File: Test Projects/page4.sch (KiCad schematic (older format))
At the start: 12 parts, among them U7 2N168

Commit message: Continued proto 1 layout
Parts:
- added C36: C, Capacitors_Tantalum_SMD:TantalC_SizeB_EIA-3528_Reflow, symbol C
- added P27, P28, P29, P30, P31, P32: CONN_01X06, Pin_Headers:Pin_Header_Straight_1x06, symbol CONN_01X06
- added R11, R12, R13, R14, R15: R, Resistors_SMD:R_0603, symbol R
- added U28, U29: SF-74x125, SparkFun-Footprints:SF-SOT-23-5, symbol SF-74x125
- added U30: SF-LM358, SparkFun-Footprints:SF-SOIC-8, symbol SF-LM358
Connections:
- net at JACK3.4: now also R11.2
- net at JACK3.5: now also R13.1
- net at JACK4.4: now also R12.2
- net at JACK4.5: now also R14.1
- net GND: now reaches U7.5 (GND)
- net GND: now also C36.1, U28.1 (/OE), U28.3 (GND), U29.1 (/OE), U29.3 (GND), U30.4 (V-)
- net PORT-TX: now reaches U7.6 (Vo)
- net PORT-TX: now also R15.2, U28.2 (A)
- net +5V: now reaches U7.8 (VCC)
- net +5V: now also C36.2, R11.1, R12.1, R15.1, U28.5 (VCC), U29.5 (VCC), U30.8 (V+)
- net at JACK5.G: now also P27.5 (P5)
- net at JACK5.R: now also P27.2 (P2)
- net at JACK5.RN: now also P27.1 (P1)
- net at JACK5.S: now also P27.6 (P6)
- net at JACK5.T: now also P27.4 (P4)
- net at JACK5.TN: now also P27.3 (P3)
- net at JACK6.G: now also P28.5 (P5)
- net at JACK6.R: now also P28.2 (P2)
- net at JACK6.RN: now also P28.1 (P1)
- net at JACK6.S: now also P28.6 (P6)
- net at JACK6.T: now also P28.4 (P4)
- net at JACK6.TN: now also P28.3 (P3)
- net at JACK7.G: now also P29.5 (P5)
- net at JACK7.R: now also P29.2 (P2)
- net at JACK7.RN: now also P29.1 (P1)
- net at JACK7.S: now also P29.6 (P6)
- net at JACK7.T: now also P29.4 (P4)
- net at JACK7.TN: now also P29.3 (P3)
- net at JACK8.G: now also P30.5 (P5)
- net at JACK8.R: now also P30.2 (P2)
- net at JACK8.RN: now also P30.1 (P1)
- net at JACK8.S: now also P30.6 (P6)
- net at JACK8.T: now also P30.4 (P4)
- net at JACK8.TN: now also P30.3 (P3)
- net at JACK9.G: now also P31.5 (P5)
- net at JACK9.R: now also P31.2 (P2)
- net at JACK9.RN: now also P31.1 (P1)
- net at JACK9.S: now also P31.6 (P6)
- net at JACK9.T: now also P31.4 (P4)
- net at JACK9.TN: now also P31.3 (P3)
- net at JACK10.G: now also P32.5 (P5)
- net at JACK10.R: now also P32.2 (P2)
- net at JACK10.RN: now also P32.1 (P1)
- net at JACK10.S: now also P32.6 (P6)
- net at JACK10.T: now also P32.4 (P4)
- net at JACK10.TN: now also P32.3 (P3)
- new net: R13.2, U28.4 (Y)
- new net: R14.2, U29.4 (Y)
- new net PORT-RX: U29.2 (A)
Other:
- moved on the sheet: JACK3, JACK4, U7

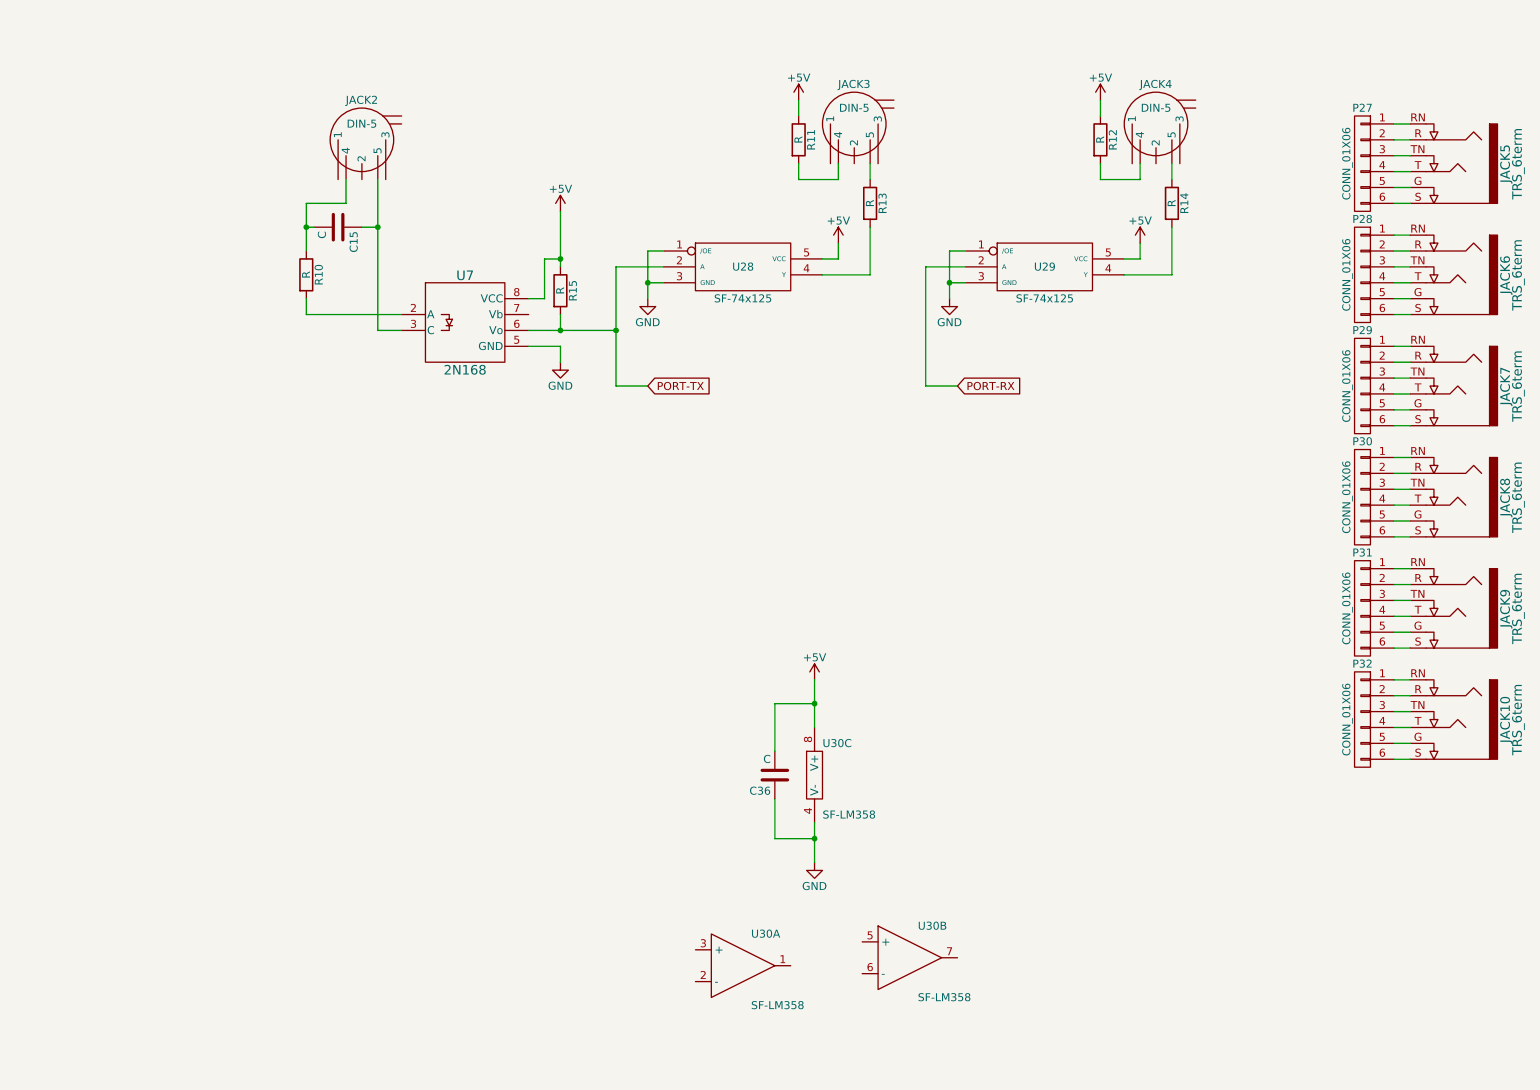
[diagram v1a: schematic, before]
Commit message: Moved to 10x5 size
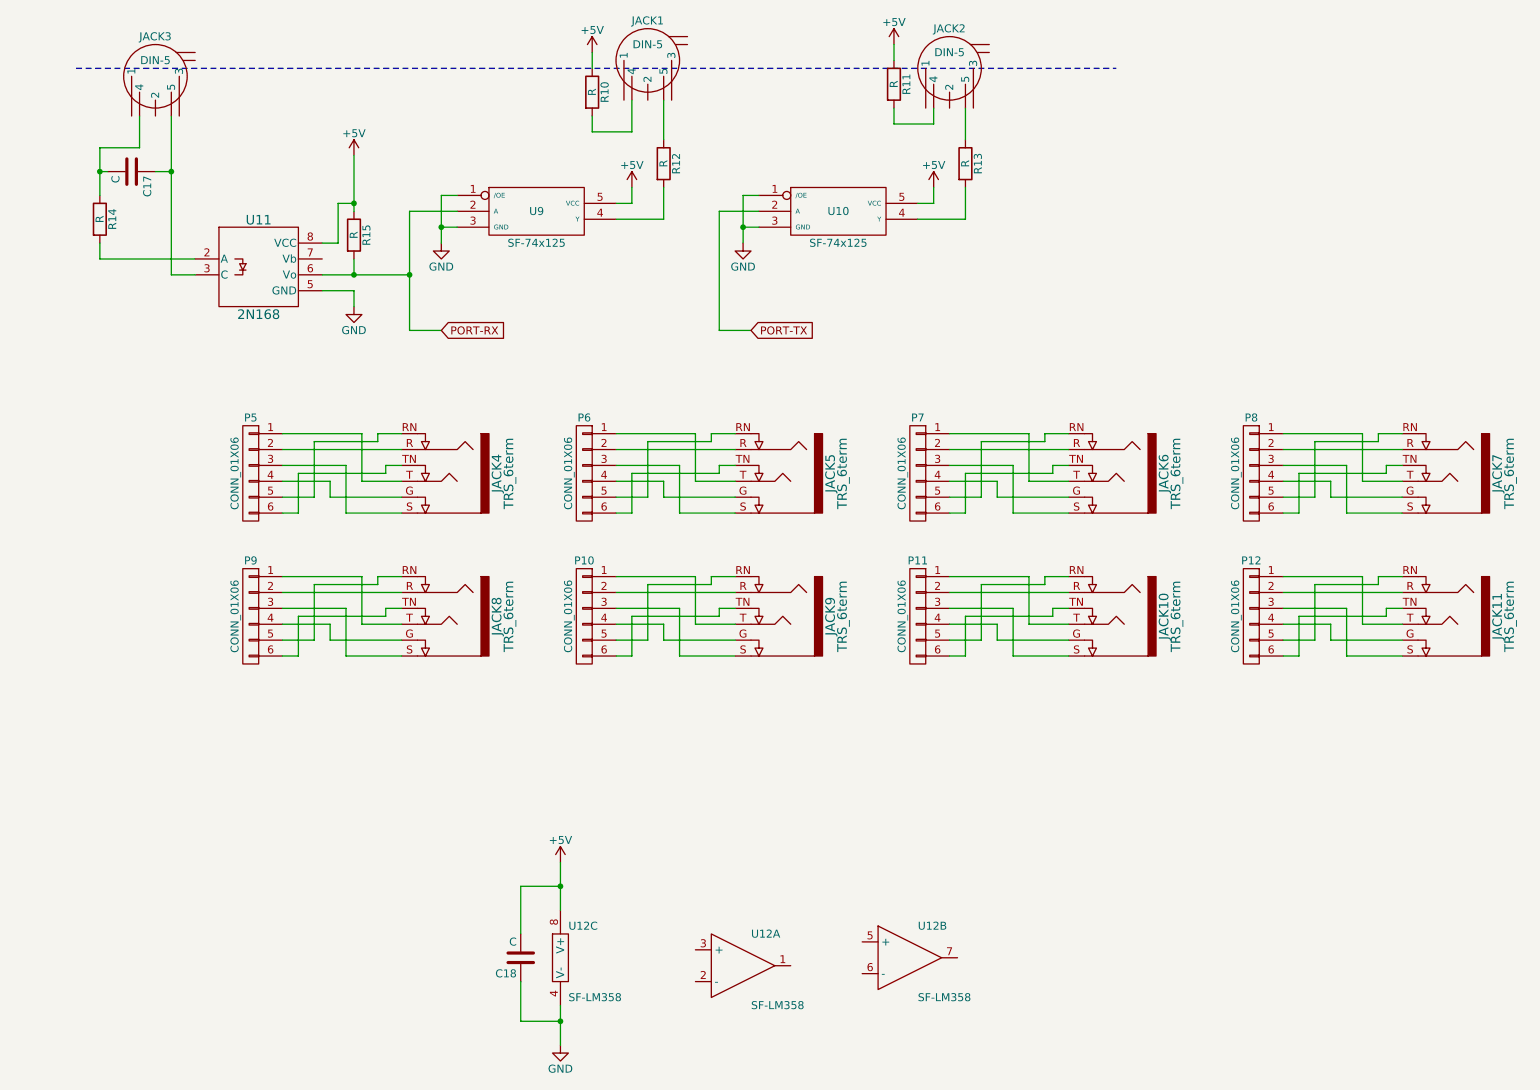
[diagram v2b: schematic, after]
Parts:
- removed P28, P29, P30, P31, P32: CONN_01X06, Pin_Headers:Pin_Header_Straight_1x06, symbol CONN_01X06
- added JACK11, JACK5: TRS_6term, SparkFun-Footprints:SF-Neutrik-Jack-6-term, symbol TRS_6term
- added P10, P11, P12, P6, P7, P8, P9: CONN_01X06, Pin_Headers:Pin_Header_Straight_1x06, symbol CONN_01X06
- renumbered C15 to C17, C36 to C18, JACK3 to JACK1, JACK4 to JACK2, JACK2 to JACK3, JACK5 to JACK4, P27 to P5, R11 to R10, R12 to R11, R13 to R12, R14 to R13, R10 to R14, U29 to U10, U7 to U11, U30 to U12, U28 to U9
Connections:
- net PORT-RX: now also R15.2, U11.6 (Vo), U9.2 (A); no longer U10.2 (A)
- net PORT-TX: now also U10.2 (A); no longer R15.2, U11.6 (Vo), U9.2 (A)
- net at JACK4.G: now also P5.4 (P4); no longer P5.5 (P5)
- net at JACK4.RN: now also P5.5 (P5); no longer P5.1 (P1)
- net at JACK4.S: now also P5.3 (P3); no longer P5.6 (P6)
- net at JACK4.T: now also P5.1 (P1); no longer P5.4 (P4)
- net at JACK4.TN: now also P5.6 (P6); no longer P5.3 (P3)
- net at JACK6.G: now also P7.4 (P4)
- net at JACK6.R: now also P7.2 (P2)
- net at JACK6.RN: now also P7.5 (P5)
- net at JACK6.S: now also P7.3 (P3)
- net at JACK6.T: now also P7.1 (P1)
- net at JACK6.TN: now also P7.6 (P6)
- net at JACK7.G: now also P8.4 (P4)
- net at JACK7.R: now also P8.2 (P2)
- net at JACK7.RN: now also P8.5 (P5)
- net at JACK7.S: now also P8.3 (P3)
- net at JACK7.T: now also P8.1 (P1)
- net at JACK7.TN: now also P8.6 (P6)
- net at JACK8.G: now also P9.4 (P4)
- net at JACK8.R: now also P9.2 (P2)
- net at JACK8.RN: now also P9.5 (P5)
- net at JACK8.S: now also P9.3 (P3)
- net at JACK8.T: now also P9.1 (P1)
- net at JACK8.TN: now also P9.6 (P6)
- net at JACK9.G: now also P10.4 (P4)
- net at JACK9.R: now also P10.2 (P2)
- net at JACK9.RN: now also P10.5 (P5)
- net at JACK9.S: now also P10.3 (P3)
- net at JACK9.T: now also P10.1 (P1)
- net at JACK9.TN: now also P10.6 (P6)
- net at JACK10.G: now also P11.4 (P4)
- net at JACK10.R: now also P11.2 (P2)
- net at JACK10.RN: now also P11.5 (P5)
- net at JACK10.S: now also P11.3 (P3)
- net at JACK10.T: now also P11.1 (P1)
- net at JACK10.TN: now also P11.6 (P6)
- new net: JACK5.G, P6.4 (P4)
- new net: JACK5.R, P6.2 (P2)
- new net: JACK5.RN, P6.5 (P5)
- new net: JACK5.S, P6.3 (P3)
- new net: JACK5.T, P6.1 (P1)
- new net: JACK5.TN, P6.6 (P6)
- new net: JACK11.G, P12.4 (P4)
- new net: JACK11.R, P12.2 (P2)
- new net: JACK11.RN, P12.5 (P5)
- new net: JACK11.S, P12.3 (P3)
- new net: JACK11.T, P12.1 (P1)
- new net: JACK11.TN, P12.6 (P6)
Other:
- moved on the sheet: C17, C18, JACK1, JACK2, JACK3, JACK4, P5, R10, R11, R12, R13, R14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

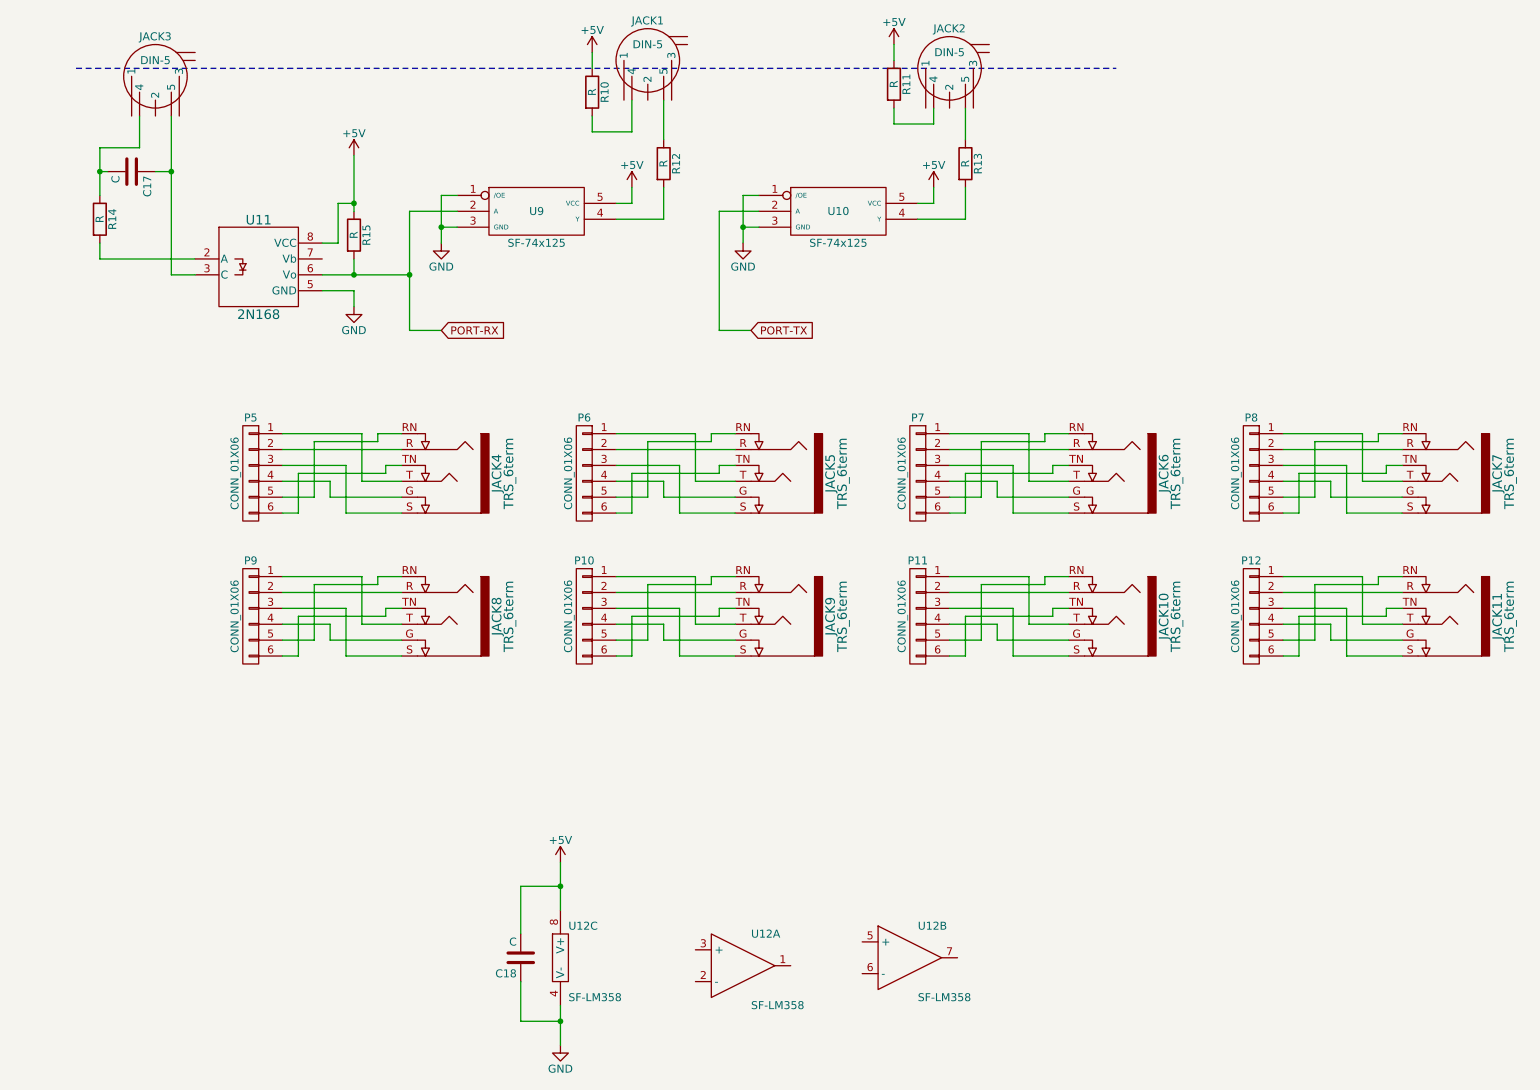
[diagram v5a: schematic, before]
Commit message: Added holes, moved layout
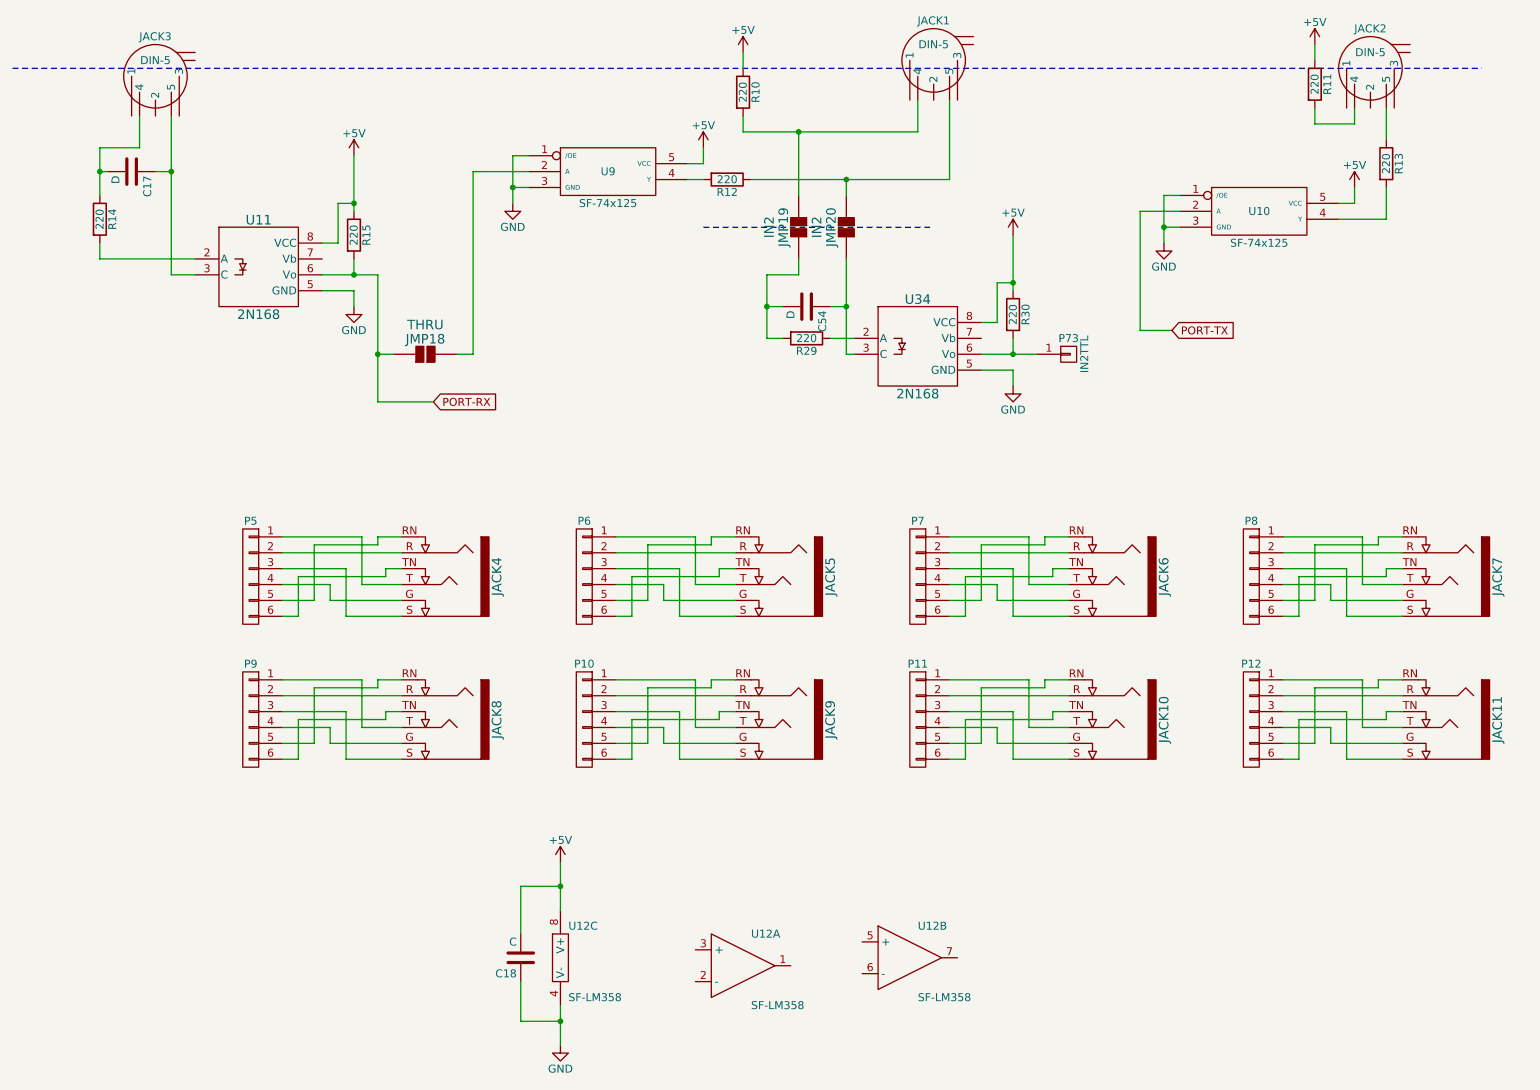
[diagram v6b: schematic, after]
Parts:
- added C54: D, Capacitors_Tantalum_SMD:TantalC_SizeB_EIA-3528_Reflow, symbol C
- added JMP18: THRU, SparkFun-Footprints:SF-2way-open, symbol 2Jumper
- added JMP19, JMP20: IN2, SparkFun-Footprints:SF-2way-open, symbol 2Jumper
- added P73: IN2TTL, SparkFun-Footprints:TestHole, symbol CONN_01X01
- added R29, R30: 220, Resistors_SMD:R_0603, symbol R
- added U34: 2N168, SparkFun-Footprints:SF-SMD-8, symbol 2N168
- C17: value C -> D
- R10, R11, R12, R13, R14, R15: value R -> 220
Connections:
- net +5V: now also R30.1, U34.8 (VCC)
- net GND: now also U34.5 (GND)
- net PORT-RX: now also JMP18.1; no longer U9.2 (A)
- net at JACK1.4, R10.2: now also JMP19.2
- net at JACK1.5, R12.1: now also JMP20.2
- new net: JMP18.2, U9.2 (A)
- new net: C54.1, JMP20.1, U34.3 (C)
- new net: C54.2, JMP19.1, R29.2
- new net: R29.1, U34.2 (A)
- new net: P73.1 (P1), R30.2, U34.6 (Vo)
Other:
- moved on the sheet: JACK1, JACK10, JACK11, JACK2, JACK4, JACK5, JACK6, JACK7, JACK8, JACK9, P10, P11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

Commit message: Routing, 15%
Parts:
- removed C18: C, Capacitors_Tantalum_SMD:TantalC_SizeB_EIA-3528_Reflow, symbol C
- removed U12: SF-LM358, SparkFun-Footprints:SF-SOIC-8, symbol SF-LM358
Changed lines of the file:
@@
 EESchema Schematic File Version 2
+LIBS:Teensy_test_layout-rescue
 LIBS:power
 LIBS:device
@@
 LIBS:SparkFun-Mounting
 LIBS:SparkFun-Opto
+LIBS:SparkFun-Connectors
 LIBS:Teensy_test_layout-cache
 EELAYER 25 0
@@
 	1    0    0    -1
 $EndComp
-$Comp
-L SF-LM358 U12
-U 1 1 568A55E7
-P 5050 6900
-F 0 "U12" H 5100 7100 50  0000 L CNN
-F 1 "SF-LM358" H 5100 6650 50  0000 L CNN
-F 2 "SparkFun-Footprints:SF-SOIC-8" H 5150 6900 50  0001 C CNN
-F 3 "" H 5150 6900 50  0000 C CNN
-	1    5050 6900
-	1    0    0    -1
-$EndComp
-$Comp
-L SF-LM358 U12
-U 2 1 568A561C
-P 6100 6850
-F 0 "U12" H 6150 7050 50  0000 L CNN
-F 1 "SF-LM358" H 6150 6600 50  0000 L CNN
-F 2 "SparkFun-Footprints:SF-SOIC-8" H 6200 6850 50  0001 C CNN
-F 3 "" H 6200 6850 50  0000 C CNN
-	2    6100 6850
-	1    0    0    -1
-$EndComp
-$Comp
-L SF-LM358 U12
-U 3 1 568A569D
-P 3900 6850
-F 0 "U12" H 3950 7050 50  0000 L CNN
-F 1 "SF-LM358" H 3950 6600 50  0000 L CNN
-F 2 "SparkFun-Footprints:SF-SOIC-8" H 4000 6850 50  0001 C CNN
-F 3 "" H 4000 6850 50  0000 C CNN
-	3    3900 6850
-	1    0    0    -1
-$EndComp
-$Comp
-L C C18
-U 1 1 568A574D
-P 3650 6850
-F 0 "C18" H 3675 6950 50  0000 L CNN
-F 1 "C" H 3675 6750 50  0000 L CNN
-F 2 "Capacitors_Tantalum_SMD:TantalC_SizeB_EIA-3528_Reflow" H 3688 6700 50  0001 C CNN
-F 3 "" H 3650 6850 50  0000 C CNN
-	1    3650 6850
-	-1   0    0    1
-$EndComp
-Wire Wire Line
-	3900 7150 3900 7400
-Wire Wire Line
-	3900 7250 3650 7250
-Wire Wire Line
-	3650 7250 3650 7000
-Wire Wire Line
-	3650 6700 3650 6400
-Wire Wire Line
-	3650 6400 3900 6400
-Wire Wire Line
-	3900 6250 3900 6550
-Connection ~ 3900 6400
-Connection ~ 3900 7250
-$Comp
-L +5V #PWR031
-U 1 1 568A5A6C
-P 3900 6250
-F 0 "#PWR031" H 3900 6100 50  0001 C CNN
-F 1 "+5V" H 3900 6390 50  0000 C CNN
-F 2 "" H 3900 6250 50  0000 C CNN
-F 3 "" H 3900 6250 50  0000 C CNN
-	1    3900 6250
-	1    0    0    -1
-$EndComp
-$Comp
-L GND #PWR032
-U 1 1 568A5AA0
-P 3900 7400
-F 0 "#PWR032" H 3900 7150 50  0001 C CNN
-F 1 "GND" H 3900 7250 50  0000 C CNN
-F 2 "" H 3900 7400 50  0000 C CNN
-F 3 "" H 3900 7400 50  0000 C CNN
-	1    3900 7400
-	1    0    0    -1
-$EndComp
